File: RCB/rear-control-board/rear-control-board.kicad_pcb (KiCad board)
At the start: 2 copper layers, 99.1 x 99.1 mm, 61 parts, among them J1 Conn_01x23, J2 Conn_01x23, J3 Conn_01x08, J4 JST-B2B-VERT-2PIN, J5 JST-B2B-VERT-2PIN, J6 FTSH-107-01-F-DV-K, K1 T9VV1K15-12S, K2 G5V-2, K3 G5V-2, Q3 Q_PMOS_GDSD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

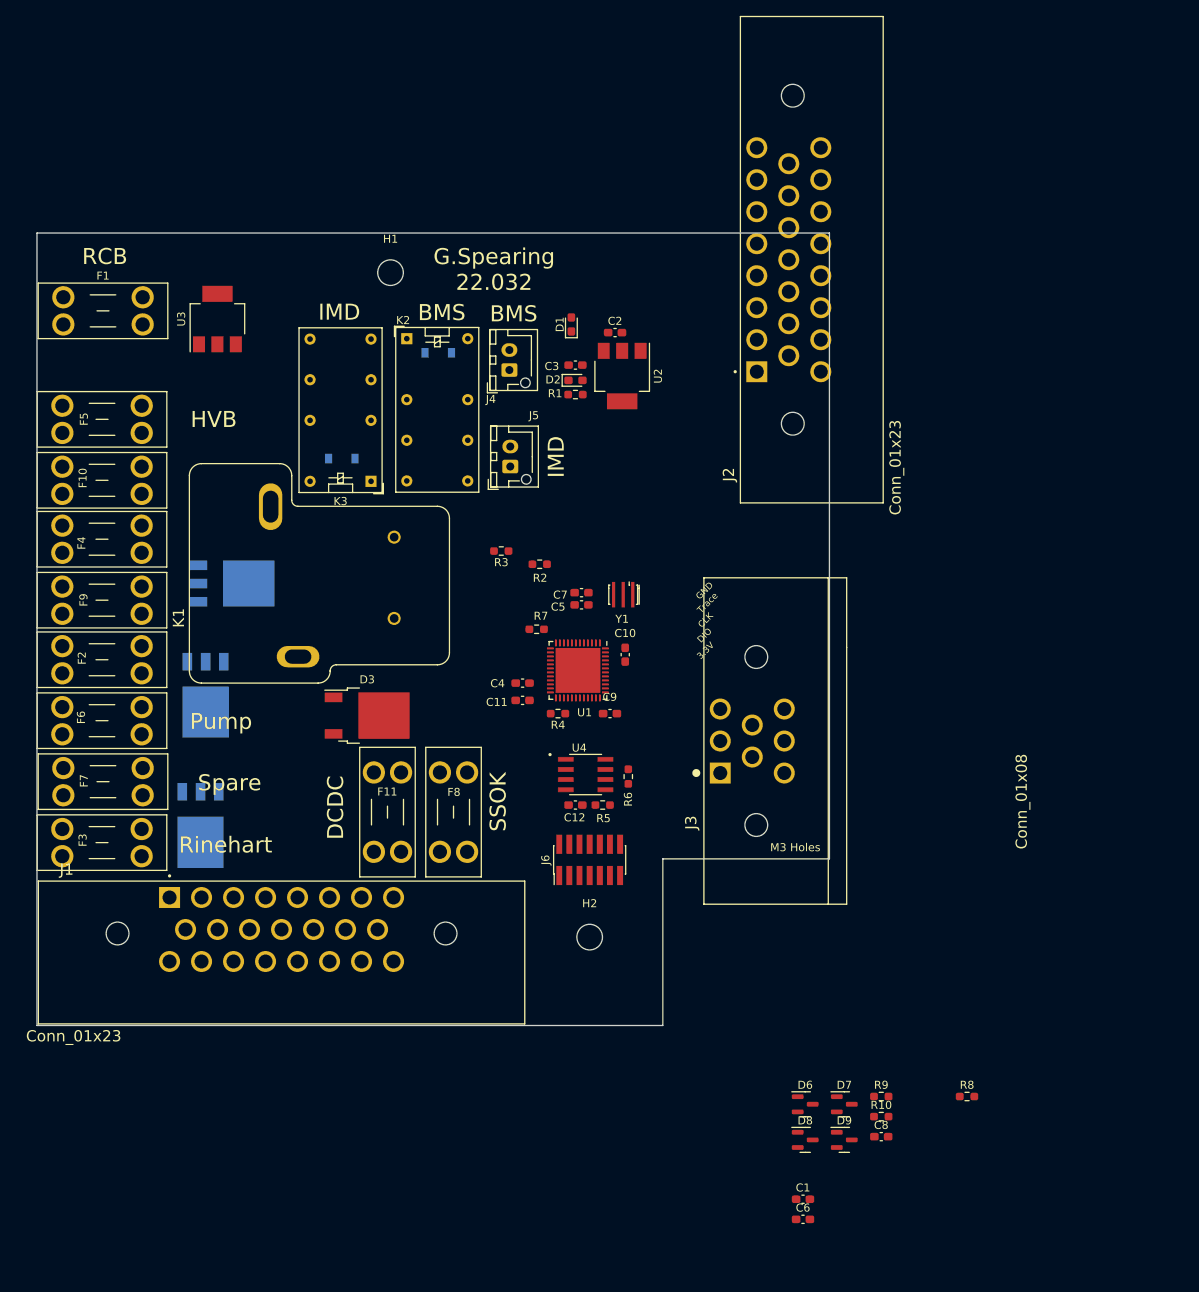
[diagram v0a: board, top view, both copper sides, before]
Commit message: minor layout changes based on schem updates
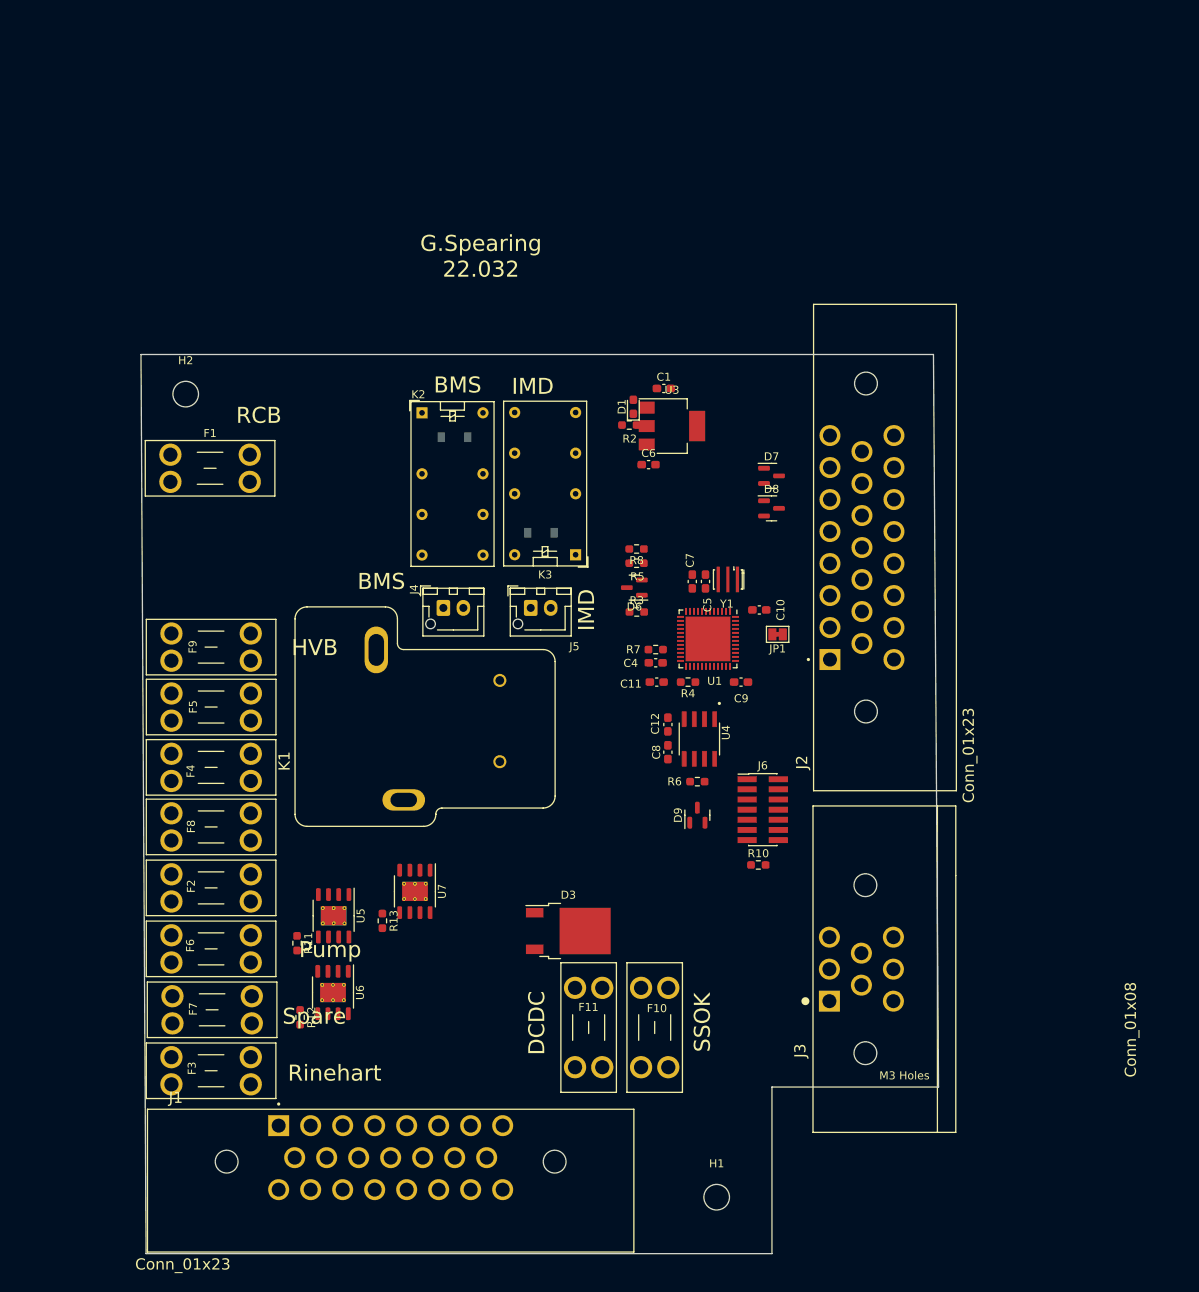
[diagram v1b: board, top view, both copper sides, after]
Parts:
- removed C2: .1u, Capacitor_SMD:C_0603_1608Metric_Pad1.08x0.95mm_HandSolder
- removed C3: 10u, Capacitor_SMD:C_0603_1608Metric_Pad1.08x0.95mm_HandSolder
- removed D2: LED, LED_SMD:LED_0603_1608Metric_Pad1.05x0.95mm_HandSolder
- removed Q3, Q4, Q5: Q_PMOS_GDSD, Package_TO_SOT_SMD:TO-252-3_TabPin4
- removed R1: 330, Resistor_SMD:R_0603_1608Metric_Pad0.98x0.95mm_HandSolder
- removed R9: 0, Resistor_SMD:R_0603_1608Metric_Pad0.98x0.95mm_HandSolder
- removed U2: LD1117S33TR_SOT223, Package_TO_SOT_SMD:SOT-223-3_TabPin2
- added JP1: SolderJumper_2_Bridged, Jumper:SolderJumper-2_P1.3mm_Bridged_Pad1.0x1.5mm, F.Cu at (153.5, 90.8)
- added R11: 1.5K, Resistor_SMD:R_0603_1608Metric_Pad0.98x0.95mm_HandSolder, F.Cu at (93.5, 129.4)
- added R12: 1.5K, Resistor_SMD:R_0603_1608Metric_Pad0.98x0.95mm_HandSolder, F.Cu at (93.9, 138.7)
- added R13: 1.5K, Resistor_SMD:R_0603_1608Metric_Pad0.98x0.95mm_HandSolder, F.Cu at (104.1, 126.6)
- added U5: BV1HAL45EFJ, Package_SO:HTSOP-8-1EP_3.9x4.9mm_P1.27mm_EP2.4x3.2mm_ThermalVias, F.Cu at (98.0, 126.0)
- added U6: BV1HAL45EFJ, Package_SO:HTSOP-8-1EP_3.9x4.9mm_P1.27mm_EP2.4x3.2mm_ThermalVias, F.Cu at (98.0, 135.6)
- added U7: BV1HAL45EFJ, Package_SO:HTSOP-8-1EP_3.9x4.9mm_P1.27mm_EP2.4x3.2mm_ThermalVias, F.Cu at (108.2, 122.9)
- moved H1 122.5 mm to (145.9, 161.2)
- moved C1 102.8 mm to (139.3, 60.1)
- moved F10 99.9 mm to (139.9, 135.0), turned to -90 degrees
- moved C6 96.3 mm to (137.4, 69.6)
- moved H2 84.6 mm to (79.6, 60.8)
- moved R8 79.9 mm to (135.9, 80.1), turned to 180 degrees
- moved D7 79.1 mm to (152.8, 71.0)
- moved D8 79.1 mm to (152.8, 75.1)
- moved D6 68.0 mm to (135.6, 85.0), turned to 180 degrees
- moved U3 58.4 mm to (140.3, 64.8), turned to 0 degrees
- moved C8 55.0 mm to (139.8, 105.5), turned to 90 degrees
- moved D9 44.5 mm to (143.5, 113.4), turned to 90 degrees
- moved F5 38.5 mm to (77.8, 98.2)
- moved F8 37.3 mm to (77.8, 113.2), turned to 0 degrees
- moved J2 37.1 mm to (160.1, 94.0)
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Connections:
- D6 pad 1: /Controller/FAULT_IMD -> /FAULT_LATCHER/BMS_SWITCH
- D6 pad 2: /FAULT_LATCHER/BMS_SWITCH -> /Controller/FAULT_IMD
- J2 pad 1: +3V3 -> unconnected-(J2-Pad1)
- J2 pad 10: /WATER_IN- -> unconnected-(J2-Pad10)
- J2 pad 11: +3V3 -> unconnected-(J2-Pad11)
- J2 pad 12: +3V3 -> unconnected-(J2-Pad12)
- J2 pad 13: /WHEEL_R -> /WHEEL_L
- J2 pad 14: /WHEEL_L -> /SUSPENSION_L
- J2 pad 15: unconnected-(J2-Pad15) -> /WATER_IN-
- J2 pad 2: +3V3 -> unconnected-(J2-Pad2)
- J2 pad 3: +3V3 -> unconnected-(J2-Pad3)
- J2 pad 4: +3V3 -> unconnected-(J2-Pad4)
- J2 pad 5: +3V3 -> unconnected-(J2-Pad5)
- J2 pad 6: +3V3 -> /WHEEL_R
- J2 pad 7: /WATER_OUT- -> /SUSPENSION_R
- J2 pad 8: /SUSPENSION_R -> /WATER_OUT-
- J2 pad 9: /SUSPENSION_L -> unconnected-(J2-Pad9)
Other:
- board size 99.1 x 99.1 mm -> 99.7 x 112.4 mm
- board text removed: "3.3V"
- board text removed: "CLK"
- board text removed: "DIO"
- board text removed: "GND"
- board text removed: "Trace"

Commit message: updating layout with schem changes
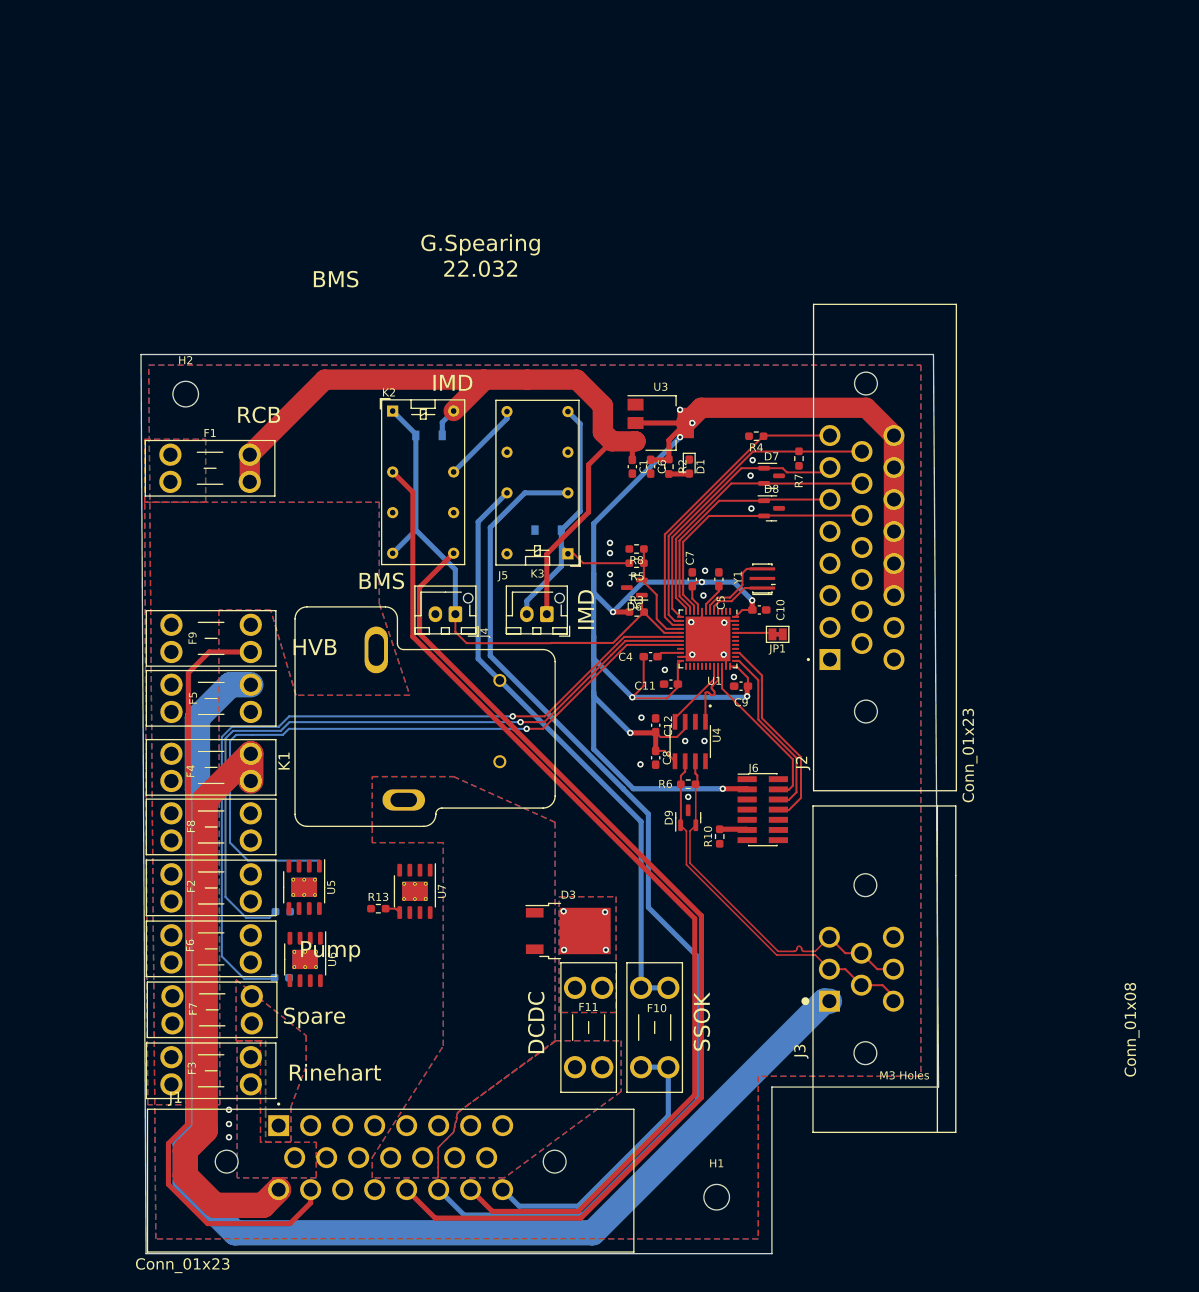
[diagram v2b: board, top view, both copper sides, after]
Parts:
- R11, R12: moved to B.Cu
- moved R4 31.9 mm to (150.9, 66.0)
- moved R7 29.8 mm to (156.2, 68.8), turned to -90 degrees
- moved C1 10.5 mm to (135.4, 69.8), turned to -90 degrees
- moved D1 10.2 mm to (142.5, 69.8), turned to -90 degrees
- moved R2 7.19 mm to (140.0, 69.8), turned to 90 degrees
- moved R10 5.99 mm to (146.3, 116.1), turned to 90 degrees
- moved R12 5.46 mm to (91.6, 133.7), turned to 0 degrees
- moved U6 5.40 mm to (94.5, 131.4)
- moved U5 5.12 mm to (94.4, 122.4)
- moved Y1 4.32 mm to (151.6, 83.8), turned to 90 degrees
- moved R11 4.32 mm to (91.7, 125.5), turned to 0 degrees
- moved K2 3.67 mm to (105.4, 62.9)
- moved D4 3.20 mm to (110.0, 65.9)
- moved J5 2.16 mm to (124.7, 88.3), turned to 180 degrees
- moved C11 1.80 mm to (140.2, 97.0)
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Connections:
- D1 pad 1: Net-(D1-Pad1) -> GND
- D1 pad 2: +3V3 -> Net-(D1-Pad2)
- F9 pad 2: /BRB_RTN -> /FuseBank/BRB_LOOP
- J1 pad 17: /BRB_RTN -> /FuseBank/BRB_LOOP
- J1 pad 20: unconnected-(J1-Pad20) -> /BRB_RTN
- J2 pad 1: unconnected-(J2-Pad1) -> GND
- J2 pad 10: unconnected-(J2-Pad10) -> GND
- J2 pad 16: unconnected-(J2-Pad16) -> GND
- J2 pad 17: unconnected-(J2-Pad17) -> GND
- J2 pad 18: GND -> +3V3
- J2 pad 19: GND -> +3V3
- J2 pad 2: unconnected-(J2-Pad2) -> GND
- J2 pad 20: GND -> +3V3
- J2 pad 21: GND -> +3V3
- J2 pad 22: GND -> +3V3
- J2 pad 23: GND -> +3V3
- J2 pad 9: unconnected-(J2-Pad9) -> GND
- K2 pad 4: /FAULT_IMD -> /FAULT_BMS
- K3 pad 4: /FAULT_BMS -> /FAULT_IMD
- R2 pad 1: GND -> Net-(D1-Pad2)
- R2 pad 2: Net-(D1-Pad1) -> +3V3
- U1 pad 14: /Controller/BRAKE_CTRL -> /WATER_IN-
- U1 pad 15: /Controller/PUMP_CTRL -> /WATER_OUT-
- U1 pad 16: /Controller/FAN_CTRL -> /Controller/FAULT_IMD
- U1 pad 17: /WATER_IN- -> /FAULT_LATCHER/BMS_SWITCH
- U1 pad 18: /Controller/FAULT_IMD -> /Controller/PUMP_CTRL
- U1 pad 19: /FAULT_LATCHER/BMS_SWITCH -> /Controller/FAN_CTRL
- U1 pad 20: unconnected-(U1-Pad20) -> /Controller/BRAKE_CTRL
- U1 pad 29: /WATER_OUT- -> unconnected-(U1-Pad29)
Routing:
- net +3V3: track 0.00 -> 236.8 mm, vias 0 -> 10
- net /REAR_12V: track 0.00 -> 162.3 mm
- net /FAULT_IMD: track 0.00 -> 133.4 mm
- net /BRB_RTN: track 0.00 -> 129.0 mm
- net /FAULT_BMS: track 0.00 -> 128.7 mm
- net /Controller/PUMP_CTRL: track 0.00 -> 97.7 mm, vias 0 -> 1
- net INT_12V: track 0.00 -> 97.2 mm
- net /FuseBank/BRB_LOOP: track 0.00 -> 96.4 mm
- net /Controller/FAN_CTRL: track 0.00 -> 89.4 mm, vias 0 -> 1
- net /Controller/BRAKE_CTRL: track 0.00 -> 86.1 mm, vias 0 -> 1
- net /SSOK: track 0.00 -> 75.2 mm
- net /FuseBank/FRONT_12V: track 0.00 -> 73.6 mm
- net /FAULT_LATCHER/BMS_SWITCH: track 0.00 -> 68.6 mm
- net /CAN_N: track 0.00 -> 46.8 mm
- net /CAN_P: track 0.00 -> 46.3 mm
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- added copper zone on B.Cu, net +12V
- added copper zone on F.Cu, net +12V
- added copper zone on B.Cu, net /BATT_12V
- added copper zone on F.Cu, net /BATT_12V
- added copper zone on B.Cu, net /DCDC_IN
- added copper zone on F.Cu, net /DCDC_IN
- added copper zone on B.Cu, net /FuseBank/RINE_12V
- added copper zone on F.Cu, net /FuseBank/RINE_12V
- added copper zone on B.Cu, net /FuseBank/SPARE_12V
- added copper zone on F.Cu, net /FuseBank/SPARE_12V
- added copper zone on B.Cu, net /charge-controller/dcdc_fuse
- added copper zone on F.Cu, net /charge-controller/dcdc_fuse
- added copper zone on B.Cu, net GND
- added copper zone on F.Cu, net GND
